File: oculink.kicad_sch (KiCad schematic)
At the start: 14 parts, among them J1 OCuLink_x4_Amphenol_G14A42121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

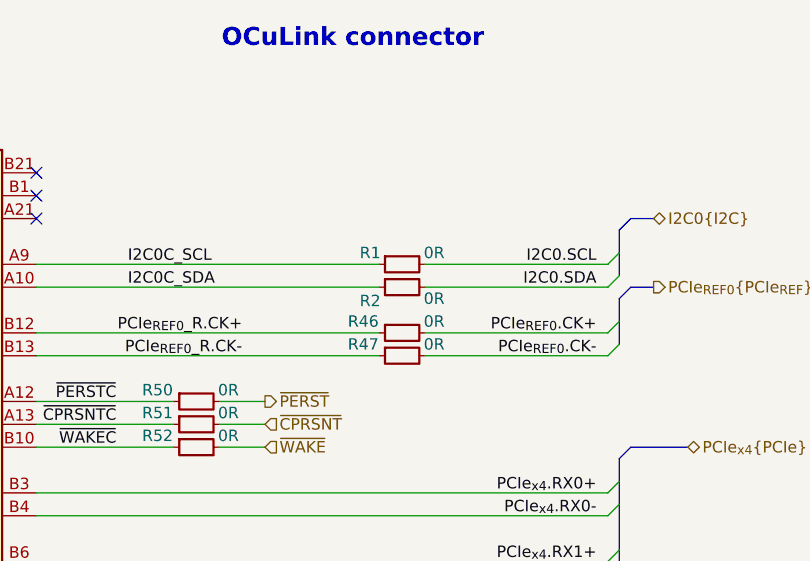
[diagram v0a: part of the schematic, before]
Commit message: [#79262] Connect all the signals
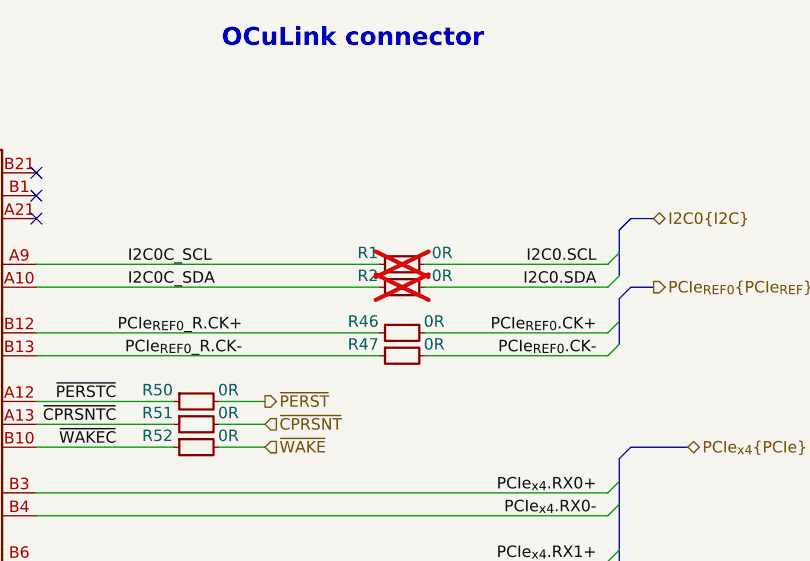
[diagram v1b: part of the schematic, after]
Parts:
- R1, R2: now not fitted
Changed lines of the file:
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@@
 		(in_bom yes)
 		(on_board yes)
-		(dnp no)
+		(dnp yes)
 		(property "Reference" "R2"
-			(at 204.724 106.934 0)
+			(at 204.47 104.14 0)
 			(effects
 				(font
@@
 		)
 		(property "Val" "0R"
-			(at 211.836 106.68 0)
+			(at 212.725 104.14 0)
 			(effects
 				(font
@@
 		(in_bom yes)
 		(on_board yes)
-		(dnp no)
+		(dnp yes)
 		(property "Reference" "R1"
-			(at 204.724 101.6 0)
+			(at 204.47 101.6 0)
 			(effects
 				(font
@@
 		)
 		(property "Val" "0R"
-			(at 211.836 101.6 0)
-			(effects
-				(font
+			(at 212.725 101.6 0)
+			(effects
+				(font

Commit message: [#79262] DRC clean
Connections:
- no-connect marks 3 -> 4
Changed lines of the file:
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@@
+	)
+	(no_connect
+		(at 246.38 210.82)
 	)
 	(no_connect

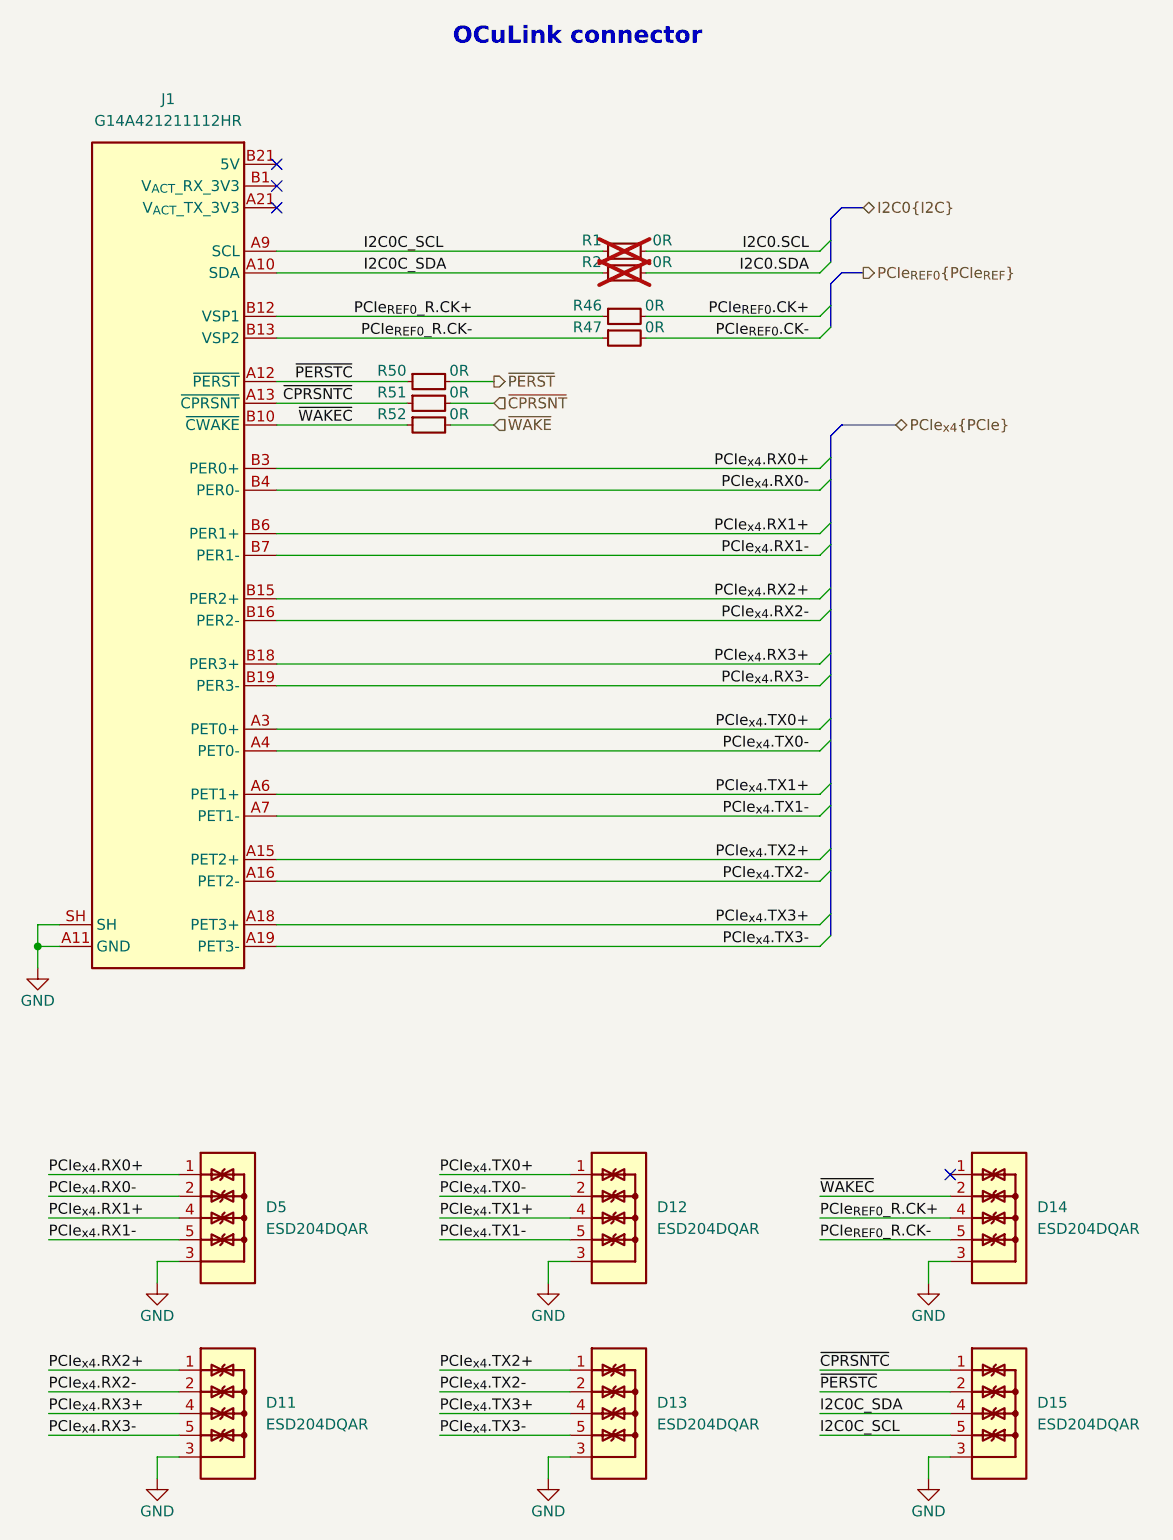
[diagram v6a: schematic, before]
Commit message: [#79790] Fixed pinout of OCuLink
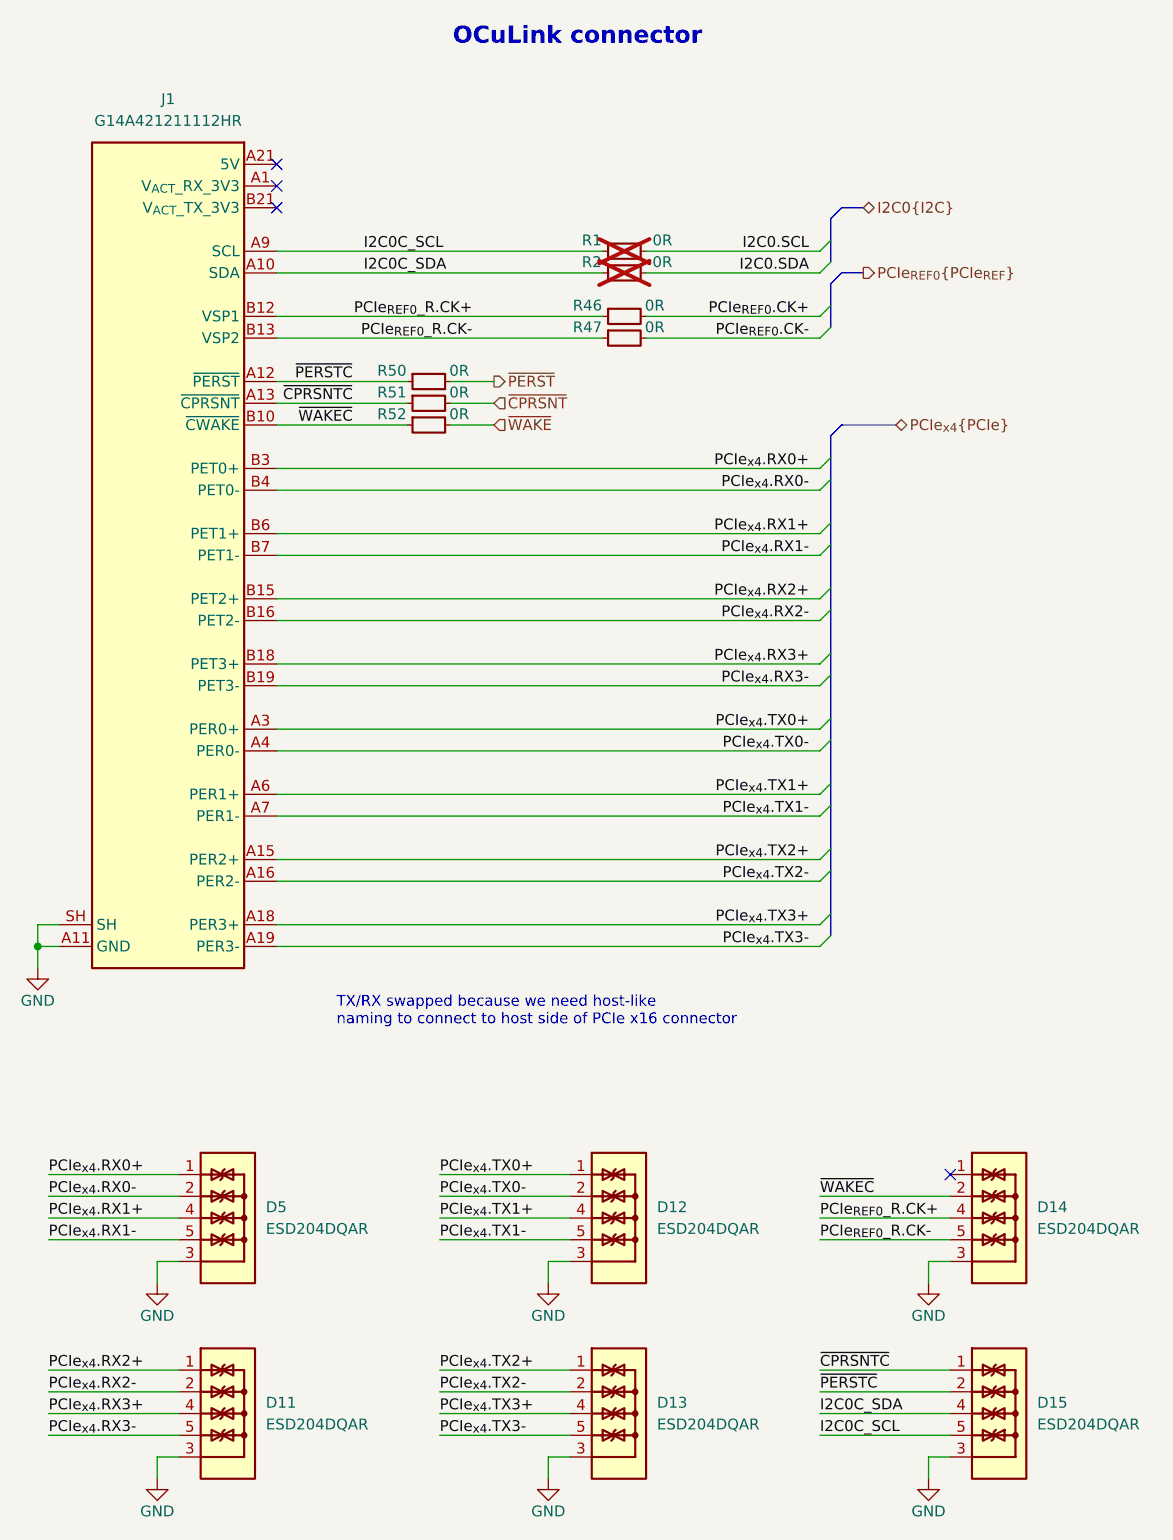
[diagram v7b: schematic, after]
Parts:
- removed J1: OCuLink_x4_Amphenol_G14A421211112HR, antmicro-footprints:Amphenol_G14A421211112HR, symbol antmicroPciConnectors:OCuLink_x4_Amphenol_G14A421211112HR_device_side
- added J1: OCuLink_x4_Amphenol_G14A421211112HR_CUSTOM_device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, antmicro-footprints:Amphenol_G14A421211112HR, symbol antmicroPciConnectors:OCuLink_x4_Amphenol_G14A421211112HR_CUSTOM_device_side
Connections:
- net GND: now also J1.A11 (GND), J1.A14 (GND), J1.A17 (GND), J1.A2 (GND), J1.A20 (GND), J1.A5 (GND), J1.A8 (GND), J1.B11 (GND), J1.B14 (GND), J1.B17 (GND), J1.B2 (GND), J1.B20 (GND), J1.B5 (GND), J1.B8 (GND), J1.SH
- net I2C0C_SCL: now also J1.A9 (SCL)
- net I2C0C_SDA: now also J1.A10 (SDA)
- net PCIe_{REF0}_R.CK+: now also J1.B12 (VSP1)
- net PCIe_{REF0}_R.CK-: now also J1.B13 (VSP2)
- net PCIe_{x4}.RX0+: now also J1.B3 (PET0+)
- net PCIe_{x4}.RX0-: now also J1.B4 (PET0-)
- net PCIe_{x4}.RX1+: now also J1.B6 (PET1+)
- net PCIe_{x4}.RX1-: now also J1.B7 (PET1-)
- net PCIe_{x4}.RX2+: now also J1.B15 (PET2+)
- net PCIe_{x4}.RX2-: now also J1.B16 (PET2-)
- net PCIe_{x4}.RX3+: now also J1.B18 (PET3+)
- net PCIe_{x4}.RX3-: now also J1.B19 (PET3-)
- net PCIe_{x4}.TX0+: now also J1.A3 (PER0+)
- net PCIe_{x4}.TX0-: now also J1.A4 (PER0-)
- net PCIe_{x4}.TX1+: now also J1.A6 (PER1+)
- net PCIe_{x4}.TX1-: now also J1.A7 (PER1-)
- net PCIe_{x4}.TX2+: now also J1.A15 (PER2+)
- net PCIe_{x4}.TX2-: now also J1.A16 (PER2-)
- net PCIe_{x4}.TX3+: now also J1.A18 (PER3+)
- net PCIe_{x4}.TX3-: now also J1.A19 (PER3-)
- net ~{CPRSNTC}: now also J1.A13 (~{CPRSNT})
- net ~{PERSTC}: now also J1.A12 (~{PERST})
- net ~{WAKEC}: now also J1.B10 (~{CWAKE})
- new net: J1.A21 (5V), J1.B1 (5V)
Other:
- note added: "TX/RX swapped because we need host-like naming to connect to host side of PCIe x16 connector"
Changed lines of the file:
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@@
 		(members "CK+" "CK-")
+	)
+	(text "TX/RX swapped because we need host-like \nnaming to connect to host side of PCIe x16 connector"
+		(exclude_from_sim no)
+		(at 174.625 191.77 0)
+		(effects
+			(font
+				(size 1.27 1.27)
+			)
+			(justify left)
+		)
 	)
 	(text "OCuLink connector"
@@
 	)
 	(symbol
+		(lib_id "antmicroPciConnectors:OCuLink_x4_Amphenol_G14A421211112HR_CUSTOM_device_side")
+		(at 167.64 92.71 0)
+		(mirror y)
+		(unit 1)
+		(exclude_from_sim no)
+		(in_bom yes)
+		(on_board yes)
+		(dnp no)
+		(fields_autoplaced yes)
+		(property "Reference" "J1"
+			(at 154.94 85.09 0)
+			(effects
+				(font
+					(size 1.27 1.27)
+					(thickness 0.15)
+				)
+			)
+		)
+		(property "Value" "OCuLink_x4_Amphenol_G14A421211112HR_CUSTOM_device_side"
+			(at 128.27 105.41 0)
+			(effects
+				(font
+					(size 1.27 1.27)
+					(thickness 0.15)
+				)
+				(justify left bottom)
+				(hide yes)
+			)
+		)
+		(property "Footprint" "antmicro-footprints:Amphenol_G14A421211112HR"
+			(at 128.27 107.95 0)
+			(effects
+				(font
+					(size 1.27 1.27)
+					(thickness 0.15)
+				)
+				(justify left bottom)
+				(hide yes)
+			)
+		)
+		(property "Datasheet" "https://cdn.amphenol-cs.com/media/wysiwyg/files/drawing/g14a421x1bxxxhr.pdf"
+			(at 128.27 110.49 0)
+			(effects
+				(font
+					(size 1.27 1.27)
+					(thickness 0.15)
+				)
+				(justify left bottom)
+				(hide yes)
+			)
+		)
+		(property "Description" "I/O Connectors OCulink, Receptacle, 0.5mm pitch, 4X, R/A SMT with shell leg SMT type, 30U\" gold plating, LCP, black, T&R packing"
+			(at 167.64 92.71 0)
+			(effects
+				(font
+					(size 1.27 1.27)
+				)
+				(hide yes)
+			)
+		)
+		(property "Manufacturer" "Amphenol"
+			(at 128.27 102.87 0)
+			(effects
+				(font
+					(size 1.27 1.27)
+					(thickness 0.15)
+				)
+				(justify left bottom)
+				(hide yes)
+			)
+		)
+		(property "MPN" "G14A421211112HR"
+			(at 154.94 87.63 0)
+			(effects
+				(font
+					(size 1.27 1.27)
+					(thickness 0.15)
+				)
+			)
+		)
+		(property "Author" "Antmicro"
+			(at 128.27 113.03 0)
+			(effects
+				(font
+					(size 1.27 1.27)
+					(thickness 0.15)
+				)
+				(justify left bottom)
+				(hide yes)
+			)
+		)
+		(property "License" "Apache-2.0"
+			(at 128.27 115.57 0)
+			(effects
+				(font
+					(size 1.27 1.27)
+					(thickness 0.15)
+				)
+				(justify left bottom)
+				(hide yes)
+			)
+		)
+		(pin "B7"
+		)
+		(pin "B9"
+		)
+		(pin "B5"
+		)
+		(pin "A13"
+		)
+		(pin "B4"
+		)
+		(pin "A16"
+		)
+		(pin "A10"
+		)
+		(pin "B12"
+		)
+		(pin "A6"
+		)
+		(pin "A2"
+		)
+		(pin "A9"
+		)
+		(pin "A7"
+		)
+		(pin "B13"
+		)
+		(pin "A1"
+		)
+		(pin "A17"
+		)
+		(pin "A4"
+		)
+		(pin "SH"
+		)
+		(pin "B11"
+		)
+		(pin "B21"
+		)
+		(pin "B2"
+		)
+		(pin "A3"
+		)
+		(pin "A15"
+		)
+		(pin "A14"
+		)
+		(pin "B14"
+		)
+		(pin "A21"
+		)
+		(pin "B1"
+		)
+		(pin "B18"
+		)
+		(pin "A11"
+		)
+		(pin "A5"
+		)
+		(pin "B3"
+		)
+		(pin "B8"
+		)
+		(pin "A20"
+		)
+		(pin "B19"
+		)
+		(pin "B10"
+		)
+		(pin "B15"
+		)
+		(pin "A8"
+		)
+		(pin "B20"
+		)
+		(pin "A12"
+		)
+		(pin "B16"
+		)
+		(pin "B6"
+		)
+		(pin "A18"
+		)
+		(pin "A19"
+		)
+		(pin "B17"
+		)
+		(instances
+			(project ""
+				(path "/44c3be85-0a18-4d93-a9a5-650ee09b6032/642de475-f425-453b-bd11-9d34133bc8d0"
+					(reference "J1")
+					(unit 1)
+				)
+			)
+		)
+	)
+	(symbol
 		(lib_id "antmicropower:GND")
 		(at 139.7 186.69 0)
@@
 					(unit 1)
 				)
-			)
-		)
-	)
-	(symbol
-		(lib_id "antmicroPciConnectors:OCuLink_x4_Amphenol_G14A421211112HR_device_side")
-		(at 167.64 92.71 0)
-		(mirror y)
-		(unit 1)
-		(exclude_from_sim no)
-		(in_bom yes)
-		(on_board yes)
-		(dnp no)
-		(fields_autoplaced yes)
-		(property "Reference" "J1"
-			(at 154.94 85.09 0)
-			(effects
-				(font
-					(size 1.27 1.27)
-					(thickness 0.15)
-				)
-			)
-		)
-		(property "Value" "OCuLink_x4_Amphenol_G14A421211112HR"
-			(at 128.27 105.41 0)
-			(effects
-				(font
-					(size 1.27 1.27)
-					(thickness 0.15)
-				)
-				(justify left bottom)
-				(hide yes)
-			)
-		)
-		(property "Footprint" "antmicro-footprints:Amphenol_G14A421211112HR"
-			(at 128.27 107.95 0)
-			(effects
-				(font
-					(size 1.27 1.27)
-					(thickness 0.15)
-				)
-				(justify left bottom)
-				(hide yes)
-			)
-		)
-		(property "Datasheet" "https://cdn.amphenol-cs.com/media/wysiwyg/files/drawing/g14a421x1bxxxhr.pdf"
-			(at 128.27 110.49 0)
-			(effects
-				(font
-					(size 1.27 1.27)
-					(thickness 0.15)
-				)
-				(justify left bottom)
-				(hide yes)
-			)
-		)
-		(property "Description" "I/O Connectors OCulink, Receptacle, 0.5mm pitch, 4X, R/A SMT with shell leg SMT type, 30U\" gold plating, LCP, black, T&R packing"
-			(at 167.64 92.71 0)
-			(effects
-				(font
-					(size 1.27 1.27)
-				)
-				(hide yes)
-			)
-		)
-		(property "Manufacturer" "Amphenol"
-			(at 128.27 102.87 0)
-			(effects
-				(font
-					(size 1.27 1.27)
-					(thickness 0.15)
-				)
-				(justify left bottom)
-				(hide yes)
-			)
-		)
-		(property "MPN" "G14A421211112HR"
-			(at 154.94 87.63 0)
-			(effects
-				(font
-					(size 1.27 1.27)
-					(thickness 0.15)
-				)
-			)
-		)
-		(property "Author" "Antmicro"
-			(at 128.27 113.03 0)
-			(effects
-				(font
-					(size 1.27 1.27)
-					(thickness 0.15)
-				)
-				(justify left bottom)
-				(hide yes)
-			)
-		)
-		(property "License" "Apache-2.0"
-			(at 128.27 115.57 0)
-			(effects
-				(font
-					(size 1.27 1.27)
-					(thickness 0.15)
-				)
-				(justify left bottom)
-				(hide yes)
-			)
-		)
-		(pin "B4"
-		)
-		(pin "A2"
-		)
-		(pin "A6"
-		)
-		(pin "A18"
-		)
-		(pin "A1"
-		)
-		(pin "A12"
-		)
-		(pin "B20"
-		)
-		(pin "A14"
-		)
-		(pin "B8"
-		)
-		(pin "A9"
-		)
-		(pin "B10"
-		)
-		(pin "A11"
-		)
-		(pin "B1"
-		)
-		(pin "A19"
-		)
-		(pin "A16"
-		)
-		(pin "B19"
-		)
-		(pin "A13"
-		)
-		(pin "B5"
-		)
-		(pin "SH"
-		)
-		(pin "B15"
-		)
-		(pin "A15"
-		)
-		(pin "B9"
-		)
-		(pin "B2"
-		)
-		(pin "B18"
-		)
-		(pin "B13"
-		)
-		(pin "B11"
-		)
-		(pin "B21"
-		)
-		(pin "A21"
-		)
-		(pin "B6"
-		)
-		(pin "A10"
-		)
-		(pin "B12"
-		)
-		(pin "A8"
-		)
-		(pin "B16"
-		)
-		(pin "B7"
-		)
-		(pin "A7"
-		)
-		(pin "B17"
-		)
-		(pin "B14"
-		)
-		(pin "A5"
-		)
-		(pin "A20"
-		)
-		(pin "A3"
-		)
-		(pin "A4"
-		)
-		(pin "B3"
-		)
-		(pin "A17"
-		)
-		(instances
-			(project ""
-				(path "/44c3be85-0a18-4d93-a9a5-650ee09b6032/642de475-f425-453b-bd11-9d34133bc8d0"
-					(reference "J1")
-					(unit 1)
-				)
